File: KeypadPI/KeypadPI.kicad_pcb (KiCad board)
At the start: 2 copper layers, 91 x 85 mm, 55 parts, among them J1 Conn_01x04, J2 Conn_02x20_Odd_Even, J3 Conn_01x01, J4 Conn_01x01, J5 Conn_01x01, J6 Conn_01x01, J7 Conn_01x04, Q1 2N7000, Q2 2N7000, SW1 SW_Push, SW10 SW_Push, SW11 SW_Push, SW12 SW_Push, SW13 SW_Push, SW14 SW_Push, SW15 SW_Push, SW16 SW_Push, SW2 SW_Push, SW3 SW_Push, SW4 SW_Push, SW5 SW_Push, SW6 SW_Push, SW7 SW_Push, SW8 SW_Push, SW9 SW_Push, U1 74HC595

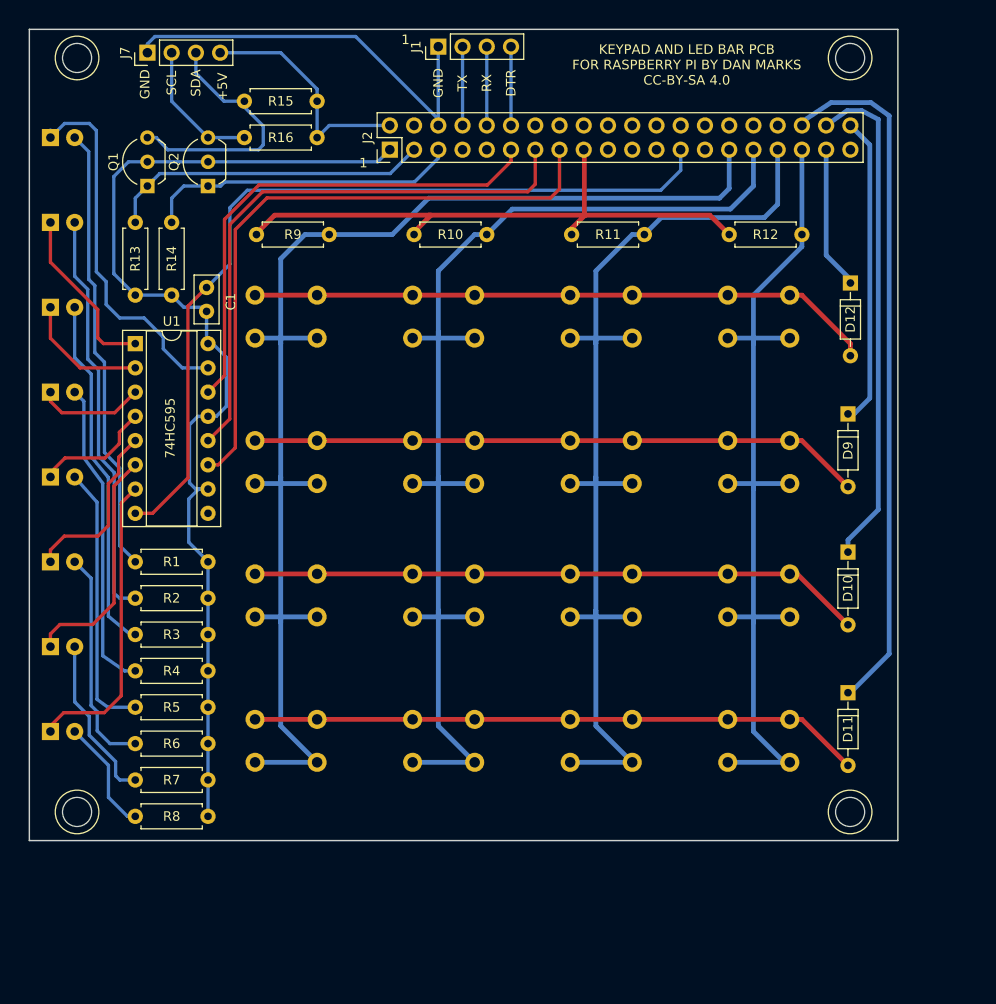
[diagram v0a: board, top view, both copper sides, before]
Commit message: Added audio input and output to keypad PCB
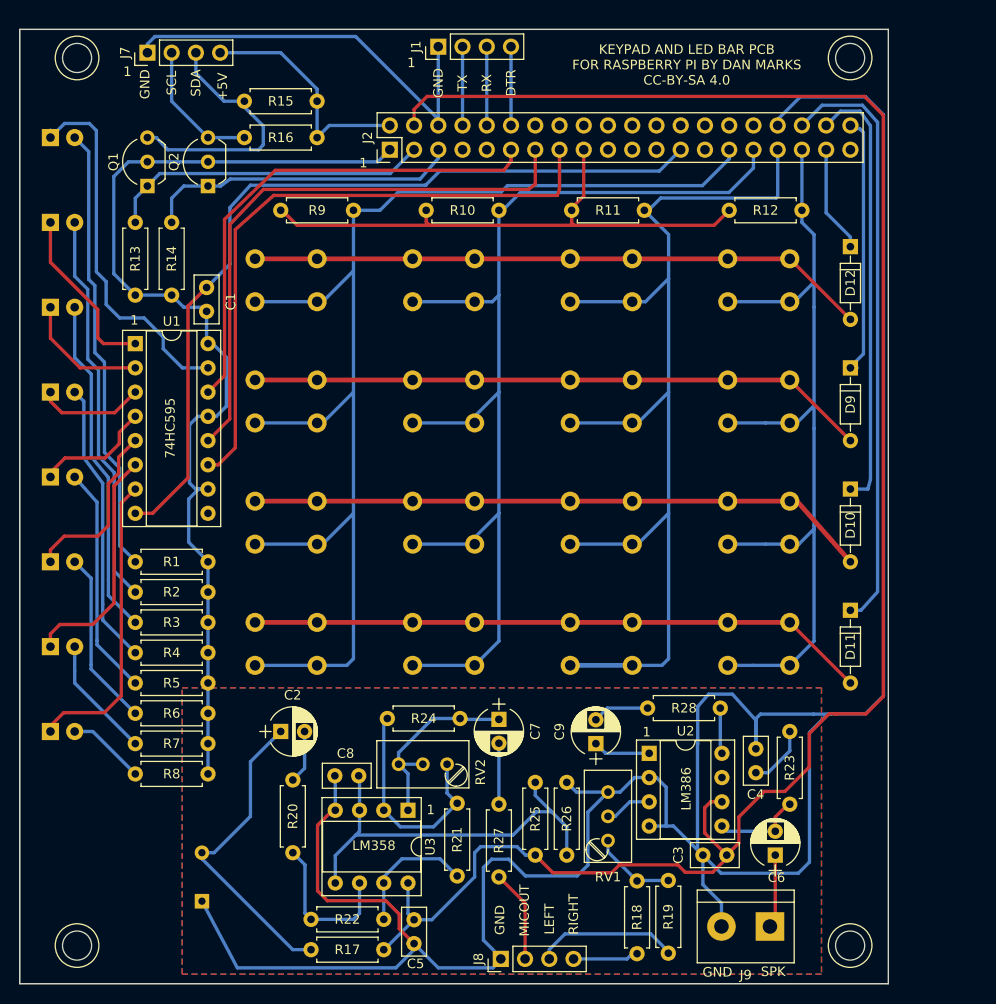
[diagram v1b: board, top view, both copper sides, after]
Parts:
- added C2: 1 uF, Capacitors_THT:CP_Radial_D5.0mm_P2.50mm, F.Cu at (53.3, 115.6)
- added C3: 100 nF, Capacitors_THT:C_Disc_D5.0mm_W2.5mm_P2.50mm, F.Cu at (100.1, 128.5)
- added C4: 100 nF, Capacitors_THT:C_Disc_D5.0mm_W2.5mm_P2.50mm, F.Cu at (103.1, 119.9)
- added C5: 100 nF, Capacitors_THT:C_Disc_D5.0mm_W2.5mm_P2.50mm, F.Cu at (67.3, 137.8)
- added C6: 220 uF, Capacitors_THT:CP_Radial_D5.0mm_P2.50mm, F.Cu at (105.2, 128.5)
- added C7: 220 uF, Capacitors_THT:CP_Radial_D5.0mm_P2.50mm, F.Cu at (76.2, 114.3)
- added C8: 100 nF, Capacitors_THT:C_Disc_D5.0mm_W2.5mm_P2.50mm, F.Cu at (59.0, 120.2)
- added C9: 10 uF, Capacitors_THT:CP_Radial_D5.0mm_P2.50mm, F.Cu at (86.4, 116.8)
- added J8: Conn_01x04, Pin_Headers:Pin_Header_Straight_1x04_Pitch2.54mm, F.Cu at (76.4, 139.4)
- added J9: SPEAKER, Connectors_Terminal_Blocks:TerminalBlock_bornier-2_P5.08mm, F.Cu at (104.6, 136.0)
- added MK1: Microphone_Condenser, KeypadPI:CondenserMic, B.Cu at (45.1, 130.8)
- added R17: 4k7, Resistors_THT:R_Axial_DIN0207_L6.3mm_D2.5mm_P7.62mm_Horizontal, F.Cu at (64.1, 138.4)
- added R18: 10k, Resistors_THT:R_Axial_DIN0207_L6.3mm_D2.5mm_P7.62mm_Horizontal, F.Cu at (90.7, 138.8)
- added R19: 10k, Resistors_THT:R_Axial_DIN0207_L6.3mm_D2.5mm_P7.62mm_Horizontal, F.Cu at (94.0, 138.8)
- added R20: 47k, Resistors_THT:R_Axial_DIN0207_L6.3mm_D2.5mm_P7.62mm_Horizontal, F.Cu at (54.6, 128.3)
- added R21: 1k, Resistors_THT:R_Axial_DIN0207_L6.3mm_D2.5mm_P7.62mm_Horizontal, F.Cu at (71.8, 123.1)
- added R22: 220k, Resistors_THT:R_Axial_DIN0207_L6.3mm_D2.5mm_P7.62mm_Horizontal, F.Cu at (64.1, 135.3)
- added R23: 10R, Resistors_THT:R_Axial_DIN0207_L6.3mm_D2.5mm_P7.62mm_Horizontal, F.Cu at (106.7, 123.2)
- added R24: NC, Resistors_THT:R_Axial_DIN0207_L6.3mm_D2.5mm_P7.62mm_Horizontal, F.Cu at (72.1, 114.2)
- added R25: 10k, Resistors_THT:R_Axial_DIN0207_L6.3mm_D2.5mm_P7.62mm_Horizontal, F.Cu at (80.0, 128.5)
- added R26: 10k, Resistors_THT:R_Axial_DIN0207_L6.3mm_D2.5mm_P7.62mm_Horizontal, F.Cu at (83.3, 128.5)
- added R27: 1k, Resistors_THT:R_Axial_DIN0207_L6.3mm_D2.5mm_P7.62mm_Horizontal, F.Cu at (76.2, 123.2)
- added R28: 1k, Resistors_THT:R_Axial_DIN0207_L6.3mm_D2.5mm_P7.62mm_Horizontal, F.Cu at (99.4, 113.1)
- added RV1: 10k, Potentiometers:Potentiometer_Trimmer_Bourns_3296W, F.Cu at (87.6, 127.0)
- added RV2: 100k, Potentiometers:Potentiometer_Trimmer_Bourns_3296W, F.Cu at (70.8, 119.0)
- added U2: LM386, Housings_DIP:DIP-8_W7.62mm_Socket, F.Cu at (91.9, 117.9)
- added U3: LM358, Housings_DIP:DIP-8_W7.62mm_Socket, F.Cu at (66.7, 123.8)
- moved J5 14.0 mm to (113.0, 138.0)
- moved J6 14.0 mm to (32.0, 138.0)
- moved SW11 10.2 mm to (90.2, 104.1)
- moved SW15 10.2 mm to (106.7, 104.1)
- moved SW3 10.2 mm to (57.1, 104.1)
- moved SW7 10.2 mm to (73.7, 104.1)
- moved D11 8.64 mm to (113.0, 102.9)
- moved SW10 7.62 mm to (90.2, 91.4)
- moved SW14 7.62 mm to (106.7, 91.4)
- moved SW2 7.62 mm to (57.1, 91.4)
- moved SW6 7.62 mm to (73.7, 91.4)
- moved D10 6.61 mm to (113.0, 90.2)
- moved SW1 6.35 mm to (57.1, 78.7)
- moved SW13 6.35 mm to (106.7, 78.7)
- moved SW5 6.35 mm to (73.7, 78.7)
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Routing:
- net /RPIGND#5: track 0.00 -> 276.6 mm
- net /RPI5V#2: track 0.00 -> 197.7 mm
- net Net-(C8-Pad2): track 0.00 -> 43.9 mm
- net Net-(C2-Pad1): track 0.00 -> 32.9 mm
- net Net-(R21-Pad1): track 0.00 -> 23.7 mm
- net Net-(C7-Pad1): track 0.00 -> 21.0 mm
- net Net-(R20-Pad1): track 0.00 -> 16.3 mm
- net Net-(J8-Pad3): track 0.00 -> 15.7 mm
- net Net-(R21-Pad2): track 0.00 -> 13.7 mm
- net Net-(J8-Pad2): track 0.00 -> 10.0 mm
- net /GPIO16: track 73.5 -> 63.7 mm
- net Net-(R18-Pad2): track 0.00 -> 9.68 mm
- net Net-(C6-Pad2): track 0.00 -> 9.38 mm
- net Net-(C6-Pad1): track 0.00 -> 8.55 mm
- net Net-(J8-Pad4): track 0.00 -> 7.45 mm
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- added copper zone on B.Cu, net /RPIGND#5
- added copper zone on F.Cu, net /RPIGND#5
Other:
- board size 91 x 85 mm -> 91 x 100 mm
- board text added: "LEFT"
- board text added: "LM358"
- board text added: "LM386"
- board text added: "MICOUT"
- board text added: "RIGHT"
- board text added: "SPK"

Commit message: Added second microphone to keypad
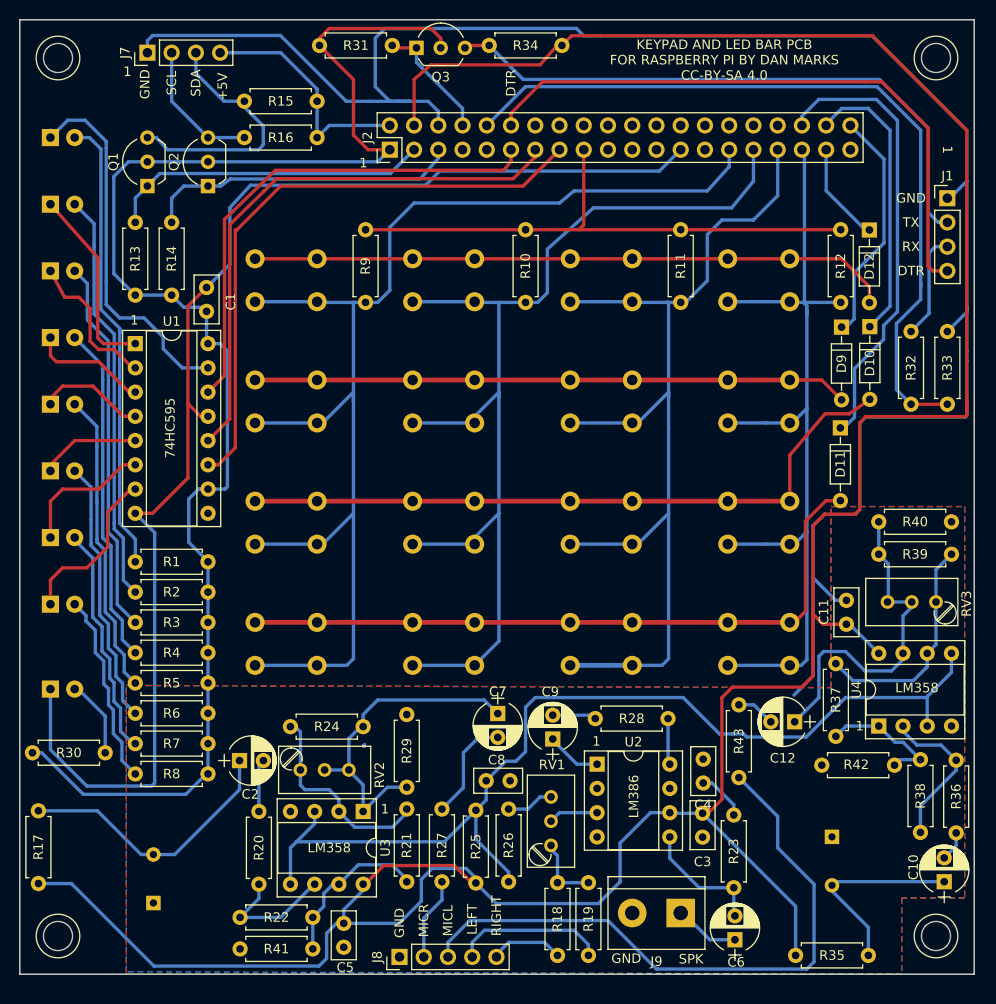
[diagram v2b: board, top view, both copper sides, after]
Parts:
- added C10: 1 uF, Capacitors_THT:CP_Radial_D5.0mm_P2.50mm, F.Cu at (122.9, 131.3)
- added C11: 100 nF, Capacitors_THT:C_Disc_D5.0mm_W2.5mm_P2.50mm, F.Cu at (112.6, 101.8)
- added C12: 220 uF, Capacitors_THT:CP_Radial_D5.0mm_P2.50mm, F.Cu at (107.2, 114.6)
- added D13: LED, LEDs:LED_D5.0mm, B.Cu at (29.2, 111.1)
- added MK2: Microphone_Condenser, KeypadPI:CondenserMic, B.Cu at (111.1, 129.2)
- added Q3: 2N7000, TO_SOT_Packages_THT:TO-92_Inline_Wide, F.Cu at (67.6, 43.9)
- added R29: 10k, Resistors_THT:R_Axial_DIN0207_L6.3mm_D2.5mm_P7.62mm_Horizontal, F.Cu at (66.5, 121.4)
- added R30: 150R, Resistors_THT:R_Axial_DIN0207_L6.3mm_D2.5mm_P7.62mm_Horizontal, F.Cu at (35.0, 117.8)
- added R31: 1k, Resistors_THT:R_Axial_DIN0207_L6.3mm_D2.5mm_P7.62mm_Horizontal, F.Cu at (57.4, 43.7)
- added R32: 470R, Resistors_THT:R_Axial_DIN0207_L6.3mm_D2.5mm_P7.62mm_Horizontal, F.Cu at (119.4, 73.7)
- added R33: 1k, Resistors_THT:R_Axial_DIN0207_L6.3mm_D2.5mm_P7.62mm_Horizontal, F.Cu at (123.2, 81.3)
- added R34: 1k, Resistors_THT:R_Axial_DIN0207_L6.3mm_D2.5mm_P7.62mm_Horizontal, F.Cu at (82.8, 43.7)
- added R35: 4k7, Resistors_THT:R_Axial_DIN0207_L6.3mm_D2.5mm_P7.62mm_Horizontal, F.Cu at (107.3, 139.0)
- added R36: 47k, Resistors_THT:R_Axial_DIN0207_L6.3mm_D2.5mm_P7.62mm_Horizontal, F.Cu at (124.1, 118.6)
- added R37: 1k, Resistors_THT:R_Axial_DIN0207_L6.3mm_D2.5mm_P7.62mm_Horizontal, F.Cu at (111.5, 108.5)
- added R38: 220k, Resistors_THT:R_Axial_DIN0207_L6.3mm_D2.5mm_P7.62mm_Horizontal, F.Cu at (120.4, 118.5)
- added R39: NC, Resistors_THT:R_Axial_DIN0207_L6.3mm_D2.5mm_P7.62mm_Horizontal, F.Cu at (116.0, 97.0)
- added R40: 10k, Resistors_THT:R_Axial_DIN0207_L6.3mm_D2.5mm_P7.62mm_Horizontal, F.Cu at (116.0, 93.6)
- added R41: 10k, Resistors_THT:R_Axial_DIN0207_L6.3mm_D2.5mm_P7.62mm_Horizontal, F.Cu at (56.7, 138.3)
- added R42: 10k, Resistors_THT:R_Axial_DIN0207_L6.3mm_D2.5mm_P7.62mm_Horizontal, F.Cu at (117.7, 119.1)
- added R43: 1k, Resistors_THT:R_Axial_DIN0207_L6.3mm_D2.5mm_P7.62mm_Horizontal, F.Cu at (101.3, 112.8)
- added RV3: 100k, Potentiometers:Potentiometer_Trimmer_Bourns_3296W, F.Cu at (122.0, 102.0)
- added U4: LM358, Housings_DIP:DIP-8_W7.62mm_Socket, F.Cu at (116.0, 115.0)
- J8: value Conn_01x04 -> Conn_01x05; footprint Pin_Headers:Pin_Header_Straight_1x04_Pitch2.54mm -> Pin_Headers:Pin_Header_Straight_1x05_Pitch2.54mm
- moved J1 55.7 mm to (123.2, 59.7), turned to 0 degrees
- moved R17 36.8 mm to (27.9, 131.5), turned to 90 degrees
- moved D11 19.1 mm to (112.0, 83.8)
- moved C8 18.4 mm to (77.4, 120.7), turned to 180 degrees
- moved D10 17.1 mm to (115.1, 73.2)
- moved RV2 15.4 mm to (55.4, 119.6), turned to 180 degrees
- moved D8 13.3 mm to (29.2, 102.2)
- moved R12 11.9 mm to (112.0, 63.0), turned to 270 degrees
- moved R11 11.6 mm to (95.2, 63.0), turned to 270 degrees
- moved D7 11.4 mm to (29.2, 95.2)
- moved J8 10.6 mm to (65.8, 139.2)
- moved R10 10.6 mm to (79.0, 63.0), turned to 270 degrees
- moved R23 10.5 mm to (100.8, 131.9)
- moved R24 10.2 mm to (62.0, 115.1)
- moved C6 9.82 mm to (100.9, 137.4)
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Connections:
- C3 pad 2: /RPIGND#5 -> /RPIGND#1
- C4 pad 2: /RPIGND#5 -> /RPIGND#1
- C5 pad 1: /RPIGND#5 -> /RPIGND#1
- C8 pad 1: /RPIGND#5 -> /RPIGND#1
- J1 pad 2: /GPIO14UART0TXD -> Net-(J1-Pad2)
- J1 pad 3: /GPIO15UART0RXD -> Net-(J1-Pad3)
- J8 pad 1: /RPIGND#5 -> /RPIGND#1
- J9 pad 2: /RPIGND#5 -> /RPIGND#1
- MK1 pad 1: /RPIGND#5 -> /RPIGND#1
- R18 pad 1: Net-(J8-Pad4) -> Net-(J8-Pad5)
- R19 pad 1: Net-(J8-Pad3) -> Net-(J8-Pad4)
- R26 pad 2: /RPIGND#5 -> /RPIGND#1
- RV1 pad 3: /RPIGND#5 -> /RPIGND#1
- U1 pad 13: VCC -> GND
- U2 pad 2: /RPIGND#5 -> /RPIGND#1
- U2 pad 4: /RPIGND#5 -> /RPIGND#1
- U3 pad 4: /RPIGND#5 -> /RPIGND#1
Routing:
- net /RPIGND#5: track 276.6 -> 0.63 mm
- net /RPIGND#1: track 44.8 -> 207.9 mm
- net /RPI5V#2: track 197.7 -> 300.4 mm
- net /GPIO15UART0RXD: track 9.05 -> 83.8 mm
- net Net-(J1-Pad2): track 0.00 -> 64.9 mm
- net Net-(C8-Pad2): track 43.9 -> 107.9 mm
- net /GPIO18PCM_CLK: track 8.26 -> 65.0 mm
- net VCC: track 107.9 -> 161.2 mm
- net GND: track 87.4 -> 138.2 mm
- net Net-(J8-Pad3): track 15.7 -> 65.8 mm
- net Net-(C12-Pad1): track 0.00 -> 36.1 mm
- net Net-(R37-Pad1): track 0.00 -> 23.8 mm
- net Net-(C10-Pad1): track 0.00 -> 20.9 mm
- net Net-(R36-Pad1): track 0.00 -> 16.5 mm
- net /GPIO20: track 46.0 -> 30.2 mm
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- added copper zone on B.Cu, net /RPIGND#1
- added copper zone on F.Cu, net /RPIGND#1
- removed copper zone on B.Cu, net /RPIGND#5
- removed copper zone on F.Cu, net /RPIGND#5
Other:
- board size 91 x 100 mm -> 100 x 100 mm
- board text added: "0"
- board text added: "2"
- board text added: "3"
- board text added: "4"
- board text added: "5"
- board text added: "6"
- board text added: "7"
- board text added: "8"
- board text added: "9"
- board text added: "DATA"
- board text added: "ENTER"
- board text added: "EXECUTE"
- board text added: "HELP"
- board text added: "LISTEN"
- board text added: "MENU"
- board text added: "MICL"
- board text added: "MICR"
- board text added: "POWER"
- board text added: "STOP"
- board text removed: "MICOUT"

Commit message: A few fixes
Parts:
- added R44: NC, Resistors_THT:R_Axial_DIN0207_L6.3mm_D2.5mm_P7.62mm_Horizontal, F.Cu at (92.7, 43.7)
- moved C2 0.41 mm to (48.6, 118.6)
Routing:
- net VCC: track 161.2 -> 178.4 mm
- net /GPIO15UART0RXD: track 83.8 -> 88.1 mm
- net /RPI5V#2: track 300.4 -> 302.8 mm
- net Net-(J1-Pad2): track 64.9 -> 66.2 mm
- net Net-(C2-Pad1): track 29.5 -> 30.1 mm
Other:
- board text added: "KEYPAD AND LED BAR V1 FOR RPI DAN MARKS CC-BY-SA 4.0"
- board text removed: "KEYPAD AND LED BAR PCB FOR RASPBERRY PI BY DAN MARKS CC-BY-SA 4.0"

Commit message: JLCPCB order 2021-10-03
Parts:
- moved R35 16.9 mm to (104.2, 122.4)
- moved MK2 2.00 mm to (110.8, 131.1), turned to 0 degrees
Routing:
- net /RPI5V#2: track 302.8 -> 292.3 mm
- net Net-(D10-Pad2): track 73.0 -> 75.7 mm
- net /RPIGND#1: track 208.1 -> 206.9 mm
- net Net-(J8-Pad3): track 65.8 -> 65.0 mm

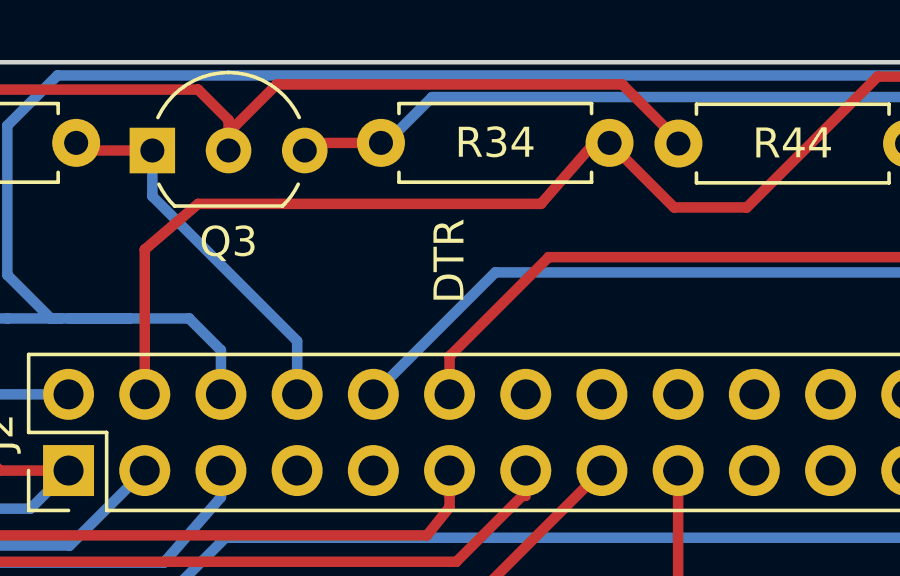
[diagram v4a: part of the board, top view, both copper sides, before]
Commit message: Begin code for controlling robot with command line
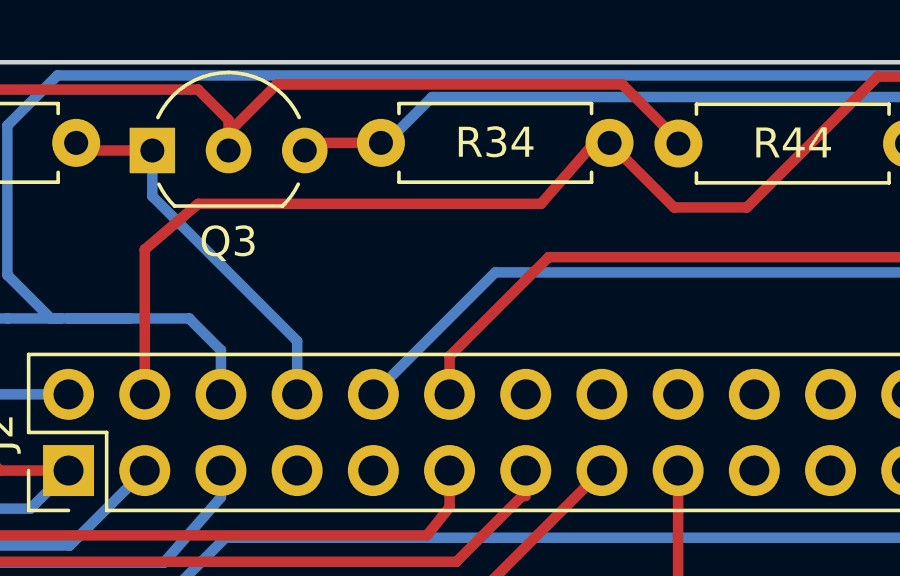
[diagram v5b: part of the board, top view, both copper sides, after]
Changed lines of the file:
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@@
     (area 25.924999 40.924999 126.075001 141.075001)
     (thickness 1.6)
-    (drawings 52)
+    (drawings 51)
     (tracks 882)
     (zones 0)
@@
   )
   (setup
-    (last_trace_width 0.35)
+    (last_trace_width 0.25)
     (user_trace_width 0.35)
     (user_trace_width 0.5)
@@
     (effects (font (size 1 1) (thickness 0.15)))
   )
-  (gr_text DTR (at 77.47 47.625 90) (layer F.SilkS)
-    (effects (font (size 1 1) (thickness 0.15)))
-  )
